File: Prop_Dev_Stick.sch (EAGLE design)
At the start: 54 parts, among them J1 10118193-0001LF, J3 M20-7822046, J4 M20-7822046, J5 M20-7820442, J6 M20-7820442, U1 P8X32A-Q44, U2 FT230XQ-R, U3 TPS2113ADRBR, U4 CAT24C512WI-GT3, U5 AD7999YRJZ-1500RL7, U6 TS2937CW33, U7 IRLML6401TRPBF, X1 ATS060CSM-1

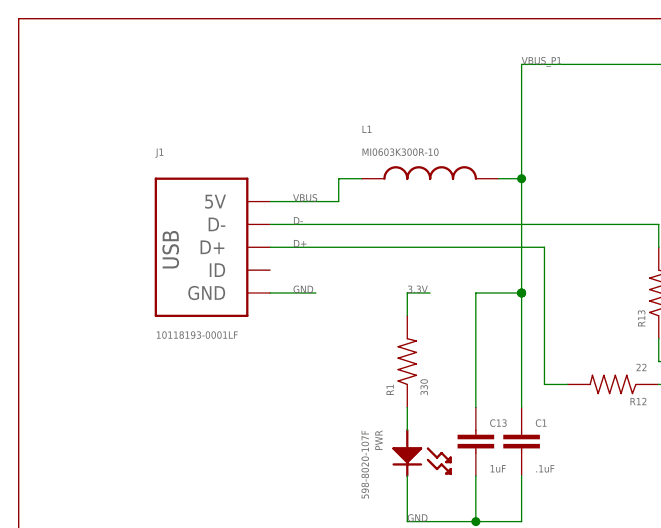
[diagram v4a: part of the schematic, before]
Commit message: Changed USB connector
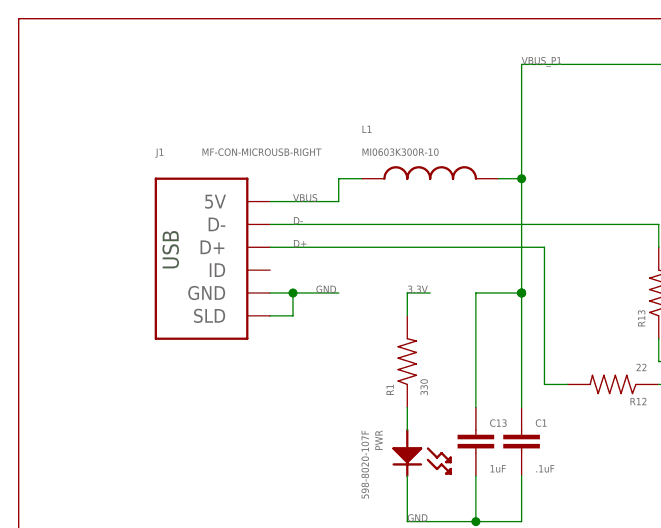
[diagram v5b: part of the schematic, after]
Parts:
- J1: value 10118193-0001LF -> MF-CON-MICROUSB-RIGHT; device PP_Connectors:USB10118193-0001LF -> MF_Connectors:USB_CON_5PRIGHT
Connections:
- net GND: now also J1.SLD
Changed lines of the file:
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@@
 <part name="R5" library="PP_Passives" deviceset="RESISTOR" device="0603" value="10K"/>
 <part name="C12" library="PP_Passives" deviceset="CAPACITOR_NON_POLAR" device="0603" value=".1uF"/>
-<part name="J1" library="PP_Connectors" deviceset="USB" device="10118193-0001LF" value="10118193-0001LF"/>
 <part name="R6" library="PP_Passives" deviceset="RESISTOR" device="0603" value="10K"/>
 <part name="R7" library="PP_Passives" deviceset="RESISTOR" device="0603" value="10K"/>
@@
 <part name="R18" library="PP_Passives" deviceset="RESISTOR" device="0603" value="25K"/>
 <part name="SD1" library="MF_Connectors" deviceset="SD_CARD_SLOT" device="RIGHT" value="MF-CON-MICROSDSLOT-RIGHT"/>
+<part name="J1" library="MF_Connectors" deviceset="USB_CON_5P" device="RIGHT" value="MF-CON-MICROUSB-RIGHT"/>
 </parts>
 <sheets>
@@
 <instance part="R5" gate="G$1" x="-261.62" y="254" rot="R90"/>
 <instance part="C12" gate="G$1" x="-269.24" y="251.46" rot="R180"/>
-<instance part="J1" gate="G$1" x="-378.46" y="251.46"/>
 <instance part="R6" gate="G$1" x="-274.32" y="213.36" rot="MR90"/>
 <instance part="R7" gate="G$1" x="-269.24" y="213.36" rot="MR90"/>
@@
 <instance part="R18" gate="G$1" x="-76.2" y="185.42" rot="R90"/>
 <instance part="SD1" gate="G$1" x="-223.52" y="190.5" rot="MR180"/>
+<instance part="J1" gate="G$1" x="-381" y="251.46"/>
 </instances>
 <busses>
@@
 </segment>
 <segment>
-<wire x1="-373.38" y1="246.38" x2="-368.3" y2="246.38" width="0.1524" layer="91"/>
-<label x="-370.84" y="246.38" size="0.8128" layer="95" font="vector"/>
+<wire x1="-373.38" y1="246.38" x2="-370.84" y2="246.38" width="0.1524" layer="91"/>
+<label x="-368.3" y="246.38" size="0.8128" layer="95" font="vector"/>
 <pinref part="J1" gate="G$1" pin="GND"/>
+<pinref part="J1" gate="G$1" pin="SLD"/>
+<wire x1="-370.84" y1="246.38" x2="-365.76" y2="246.38" width="0.1524" layer="91"/>
+<wire x1="-373.38" y1="243.84" x2="-370.84" y2="243.84" width="0.1524" layer="91"/>
+<wire x1="-370.84" y1="243.84" x2="-370.84" y2="246.38" width="0.1524" layer="91"/>
+<junction x="-370.84" y="246.38"/>
 </segment>
 <segment>
@@
 <net name="VBUS" class="0">
 <segment>
-<pinref part="J1" gate="G$1" pin="5V"/>
 <wire x1="-373.38" y1="256.54" x2="-365.76" y2="256.54" width="0.1524" layer="91"/>
 <wire x1="-365.76" y1="256.54" x2="-365.76" y2="259.08" width="0.1524" layer="91"/>
@@
 <pinref part="L1" gate="G$1" pin="P$1"/>
 <wire x1="-365.76" y1="259.08" x2="-363.22" y2="259.08" width="0.1524" layer="91"/>
+<pinref part="J1" gate="G$1" pin="5V"/>
 </segment>
 </net>
@@
 <wire x1="-373.38" y1="251.46" x2="-342.9" y2="251.46" width="0.1524" layer="91"/>
 <label x="-370.84" y="251.46" size="0.8128" layer="95" font="vector"/>
-<pinref part="J1" gate="G$1" pin="D+"/>
 <wire x1="-342.9" y1="251.46" x2="-342.9" y2="236.22" width="0.1524" layer="91"/>
 <pinref part="R12" gate="G$1" pin="2"/>
 <wire x1="-342.9" y1="236.22" x2="-340.36" y2="236.22" width="0.1524" layer="91"/>
+<pinref part="J1" gate="G$1" pin="D+"/>
 </segment>
 </net>
@@
 <net name="D-" class="0">
 <segment>
-<pinref part="J1" gate="G$1" pin="D-"/>
 <label x="-370.84" y="254" size="0.8128" layer="95" font="vector"/>
 <wire x1="-373.38" y1="254" x2="-330.2" y2="254" width="0.1524" layer="91"/>
 <pinref part="R13" gate="G$1" pin="2"/>
 <wire x1="-330.2" y1="254" x2="-330.2" y2="251.46" width="0.1524" layer="91"/>
-</segment>
-</net>
+<pinref part="J1" gate="G$1" pin="D-"/>
+</segment>
+</net>

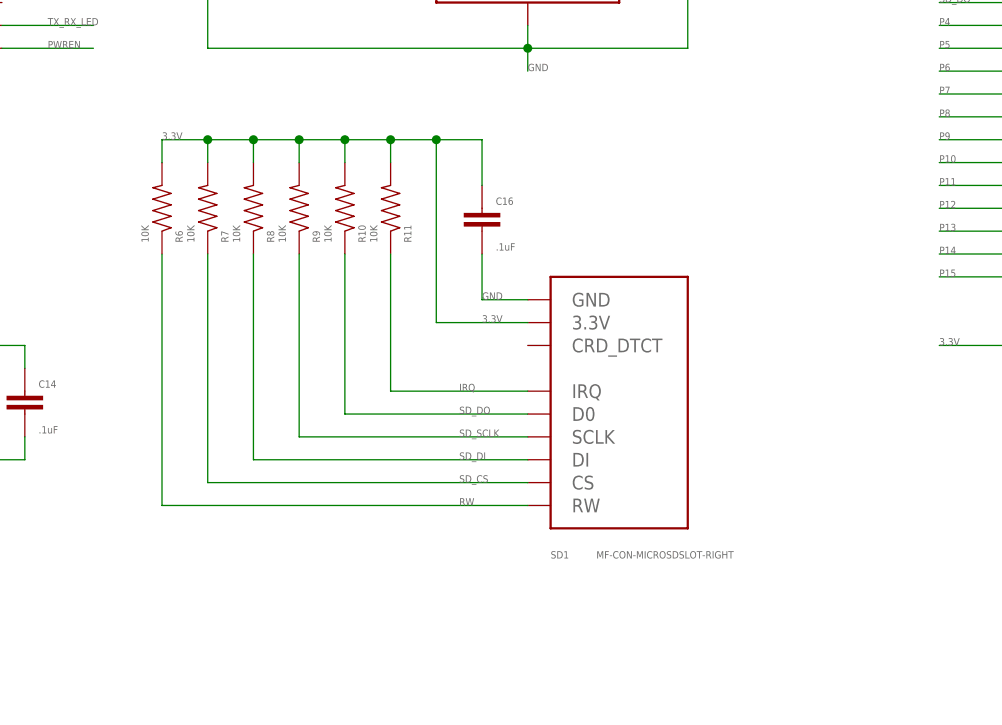
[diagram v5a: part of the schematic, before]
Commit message: Routed power switching for LDO dropout
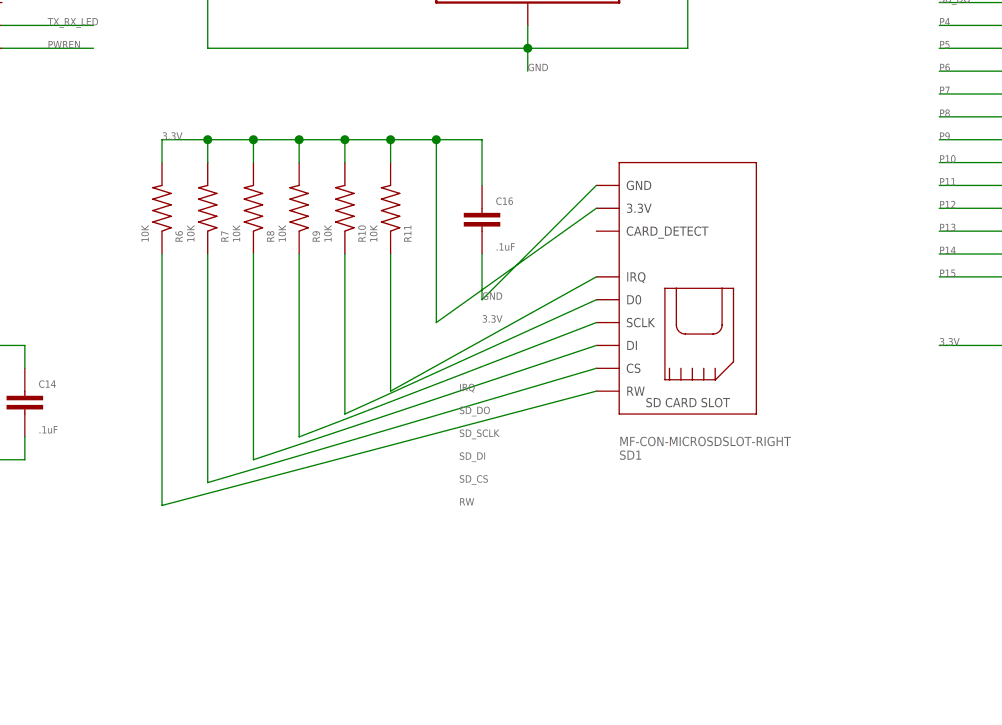
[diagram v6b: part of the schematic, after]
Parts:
- SD1: device MF_Connectors:SD_CARD_SLOTRIGHT -> MF_Connectors:SD_CARD_SLOT_MICRO_RIGHT
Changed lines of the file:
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@@
 <part name="R3" library="PP_Passives" deviceset="RESISTOR" device="0603" value="100K"/>
 <part name="R18" library="PP_Passives" deviceset="RESISTOR" device="0603" value="25K"/>
-<part name="SD1" library="MF_Connectors" deviceset="SD_CARD_SLOT" device="RIGHT" value="MF-CON-MICROSDSLOT-RIGHT"/>
+<part name="SD1" library="MF_Connectors" deviceset="SD_CARD_SLOT" device="_MICRO_RIGHT" value="MF-CON-MICROSDSLOT-RIGHT"/>
 <part name="J1" library="MF_Connectors" deviceset="USB_CON_5P" device="RIGHT" value="MF-CON-MICROUSB-RIGHT"/>
 </parts>
@@
 </segment>
 <segment>
-<wire x1="-233.68" y1="203.2" x2="-238.76" y2="203.2" width="0.1524" layer="91"/>
+<wire x1="-226.06" y1="215.9" x2="-238.76" y2="203.2" width="0.1524" layer="91"/>
 <label x="-238.76" y="203.2" size="0.8128" layer="95" font="vector"/>
 <pinref part="C16" gate="G$1" pin="2"/>
@@
 <wire x1="-248.92" y1="220.98" x2="-243.84" y2="220.98" width="0.1524" layer="91"/>
 <wire x1="-243.84" y1="220.98" x2="-243.84" y2="200.66" width="0.1524" layer="91"/>
-<wire x1="-243.84" y1="200.66" x2="-233.68" y2="200.66" width="0.1524" layer="91"/>
+<wire x1="-243.84" y1="200.66" x2="-226.06" y2="213.36" width="0.1524" layer="91"/>
 <label x="-238.76" y="200.66" size="0.8128" layer="95" font="vector"/>
 <label x="-274.32" y="220.98" size="0.8128" layer="95" font="vector"/>
@@
 <net name="SD_SCLK" class="0">
 <segment>
-<wire x1="-233.68" y1="187.96" x2="-259.08" y2="187.96" width="0.1524" layer="91"/>
+<wire x1="-226.06" y1="200.66" x2="-259.08" y2="187.96" width="0.1524" layer="91"/>
 <label x="-241.3" y="187.96" size="0.8128" layer="95" font="vector"/>
 <pinref part="R9" gate="G$1" pin="1"/>
@@
 <net name="SD_DI" class="0">
 <segment>
-<wire x1="-233.68" y1="185.42" x2="-264.16" y2="185.42" width="0.1524" layer="91"/>
+<wire x1="-226.06" y1="198.12" x2="-264.16" y2="185.42" width="0.1524" layer="91"/>
 <label x="-241.3" y="185.42" size="0.8128" layer="95" font="vector"/>
 <pinref part="R8" gate="G$1" pin="1"/>
@@
 <net name="SD_CS" class="0">
 <segment>
-<wire x1="-233.68" y1="182.88" x2="-269.24" y2="182.88" width="0.1524" layer="91"/>
+<wire x1="-226.06" y1="195.58" x2="-269.24" y2="182.88" width="0.1524" layer="91"/>
 <label x="-241.3" y="182.88" size="0.8128" layer="95" font="vector"/>
 <pinref part="R7" gate="G$1" pin="1"/>
@@
 <net name="IRQ" class="0">
 <segment>
-<wire x1="-233.68" y1="193.04" x2="-248.92" y2="193.04" width="0.1524" layer="91"/>
+<wire x1="-226.06" y1="205.74" x2="-248.92" y2="193.04" width="0.1524" layer="91"/>
 <label x="-241.3" y="193.04" size="0.8128" layer="95" font="vector"/>
 <pinref part="R11" gate="G$1" pin="1"/>
@@
 <net name="RW" class="0">
 <segment>
-<wire x1="-233.68" y1="180.34" x2="-274.32" y2="180.34" width="0.1524" layer="91"/>
+<wire x1="-226.06" y1="193.04" x2="-274.32" y2="180.34" width="0.1524" layer="91"/>
 <label x="-241.3" y="180.34" size="0.8128" layer="95" font="vector"/>
 <pinref part="R6" gate="G$1" pin="1"/>
@@
 <net name="SD_DO" class="0">
 <segment>
-<wire x1="-233.68" y1="190.5" x2="-254" y2="190.5" width="0.1524" layer="91"/>
+<wire x1="-226.06" y1="203.2" x2="-254" y2="190.5" width="0.1524" layer="91"/>
 <label x="-241.3" y="190.5" size="0.8128" layer="95" font="vector"/>
 <pinref part="R10" gate="G$1" pin="1"/>
